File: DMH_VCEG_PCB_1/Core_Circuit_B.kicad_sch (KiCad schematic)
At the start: 104 parts, among them J24 Conn_01x06_PinHeader, J25 Conn_01x10_PinHeader, J26 Conn_01x10_PinHeader, Q17 BC558, Q18 BC558, Q19 BC548, Q20 BC548, Q21 BS170, Q22 BS170, Q23 BC548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

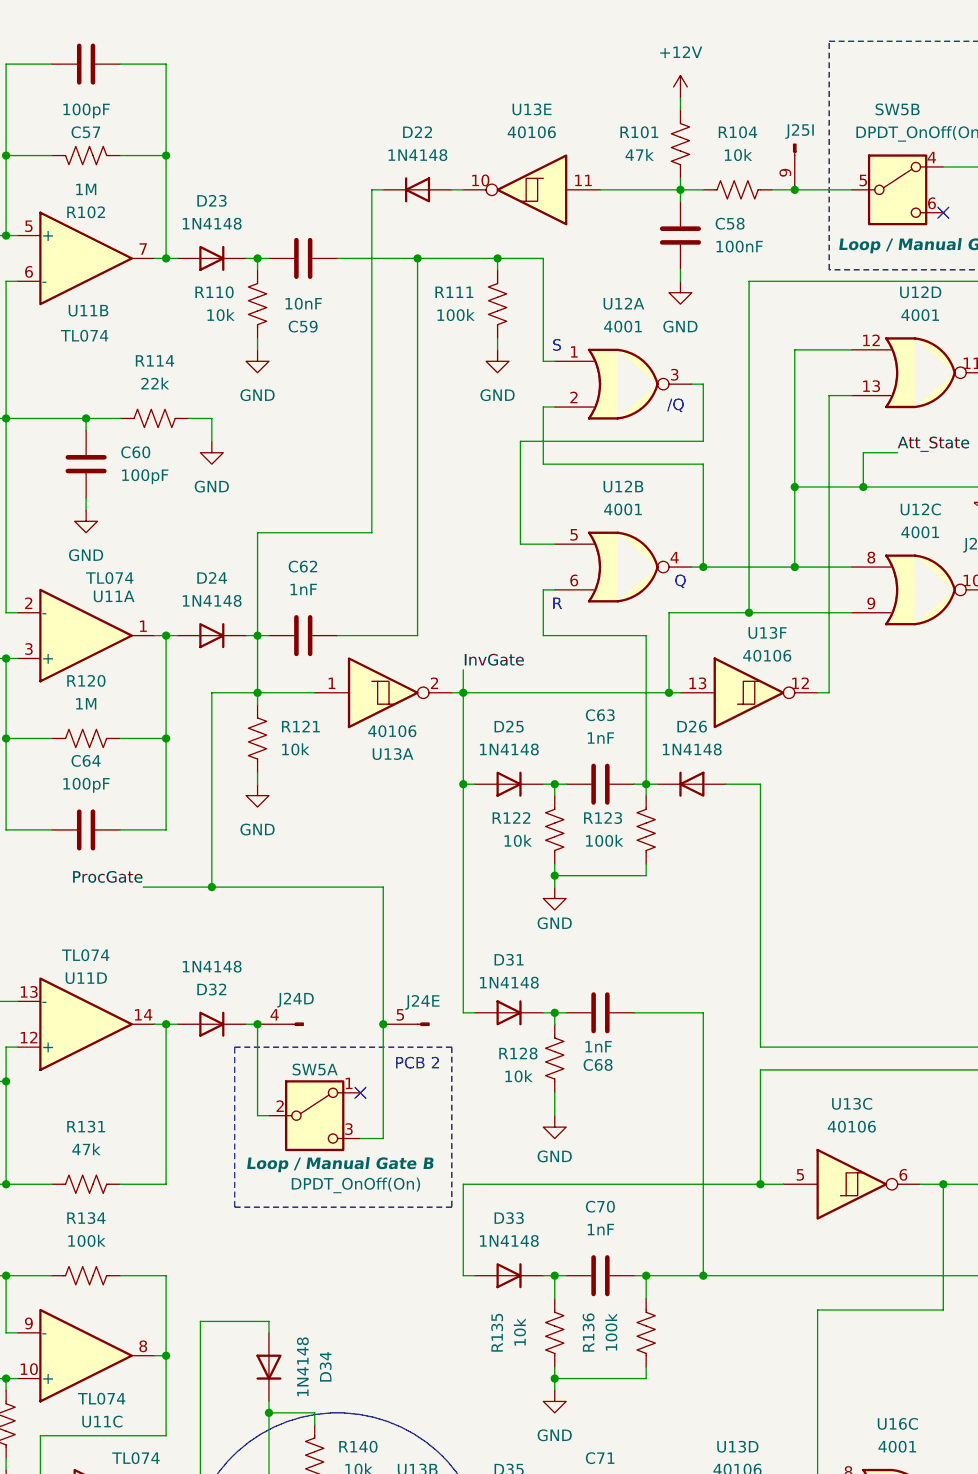
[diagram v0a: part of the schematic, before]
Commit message: Updated PCB 1 with changes from breadboard tests
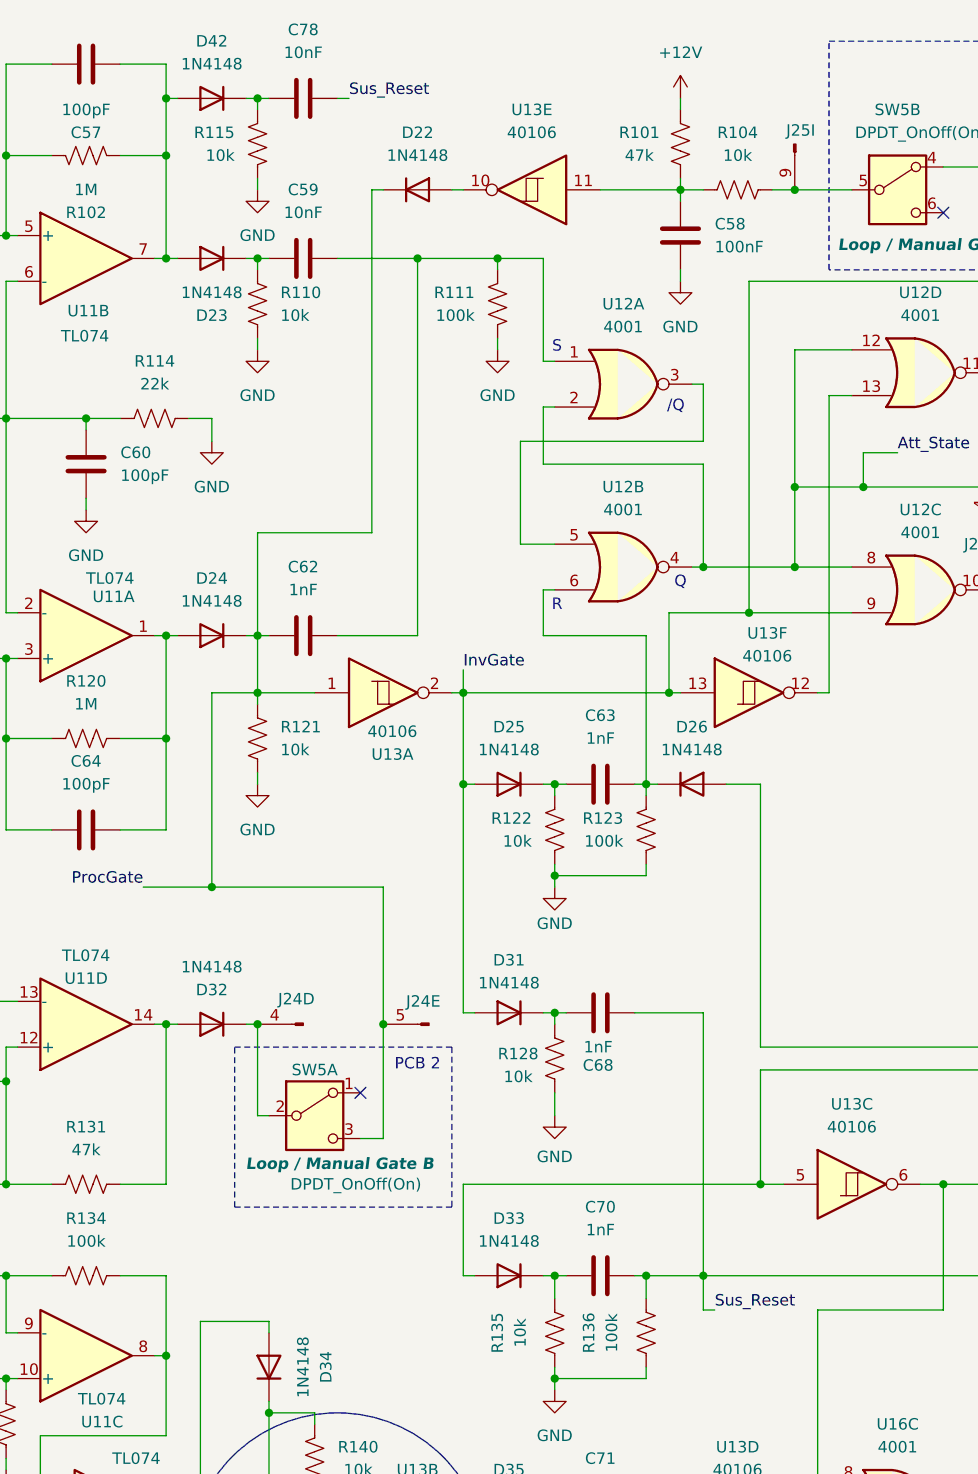
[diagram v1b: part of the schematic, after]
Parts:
- added C78: 10nF, Capacitor_THT:C_Disc_D4.3mm_W1.9mm_P5.00mm, symbol Device:C
- added D42: 1N4148, Diode_THT:D_DO-35_SOD27_P7.62mm_Horizontal, symbol Diode:1N4148
- added R115: 10k, Resistor_THT:R_Axial_DIN0207_L6.3mm_D2.5mm_P7.62mm_Horizontal, symbol Device:R_US
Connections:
- net GND: now also R115.1
- net at C57.2, D23.2 (A), R102.1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: now also D42.2 (A)
- net Sus_Reset: now reaches C68.2, C70.2, R136.1, U16.1
- net Sus_Reset: now also C78.2
- new net: C78.1, D42.1 (K), R115.2
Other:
- moved on the sheet: D23, R110

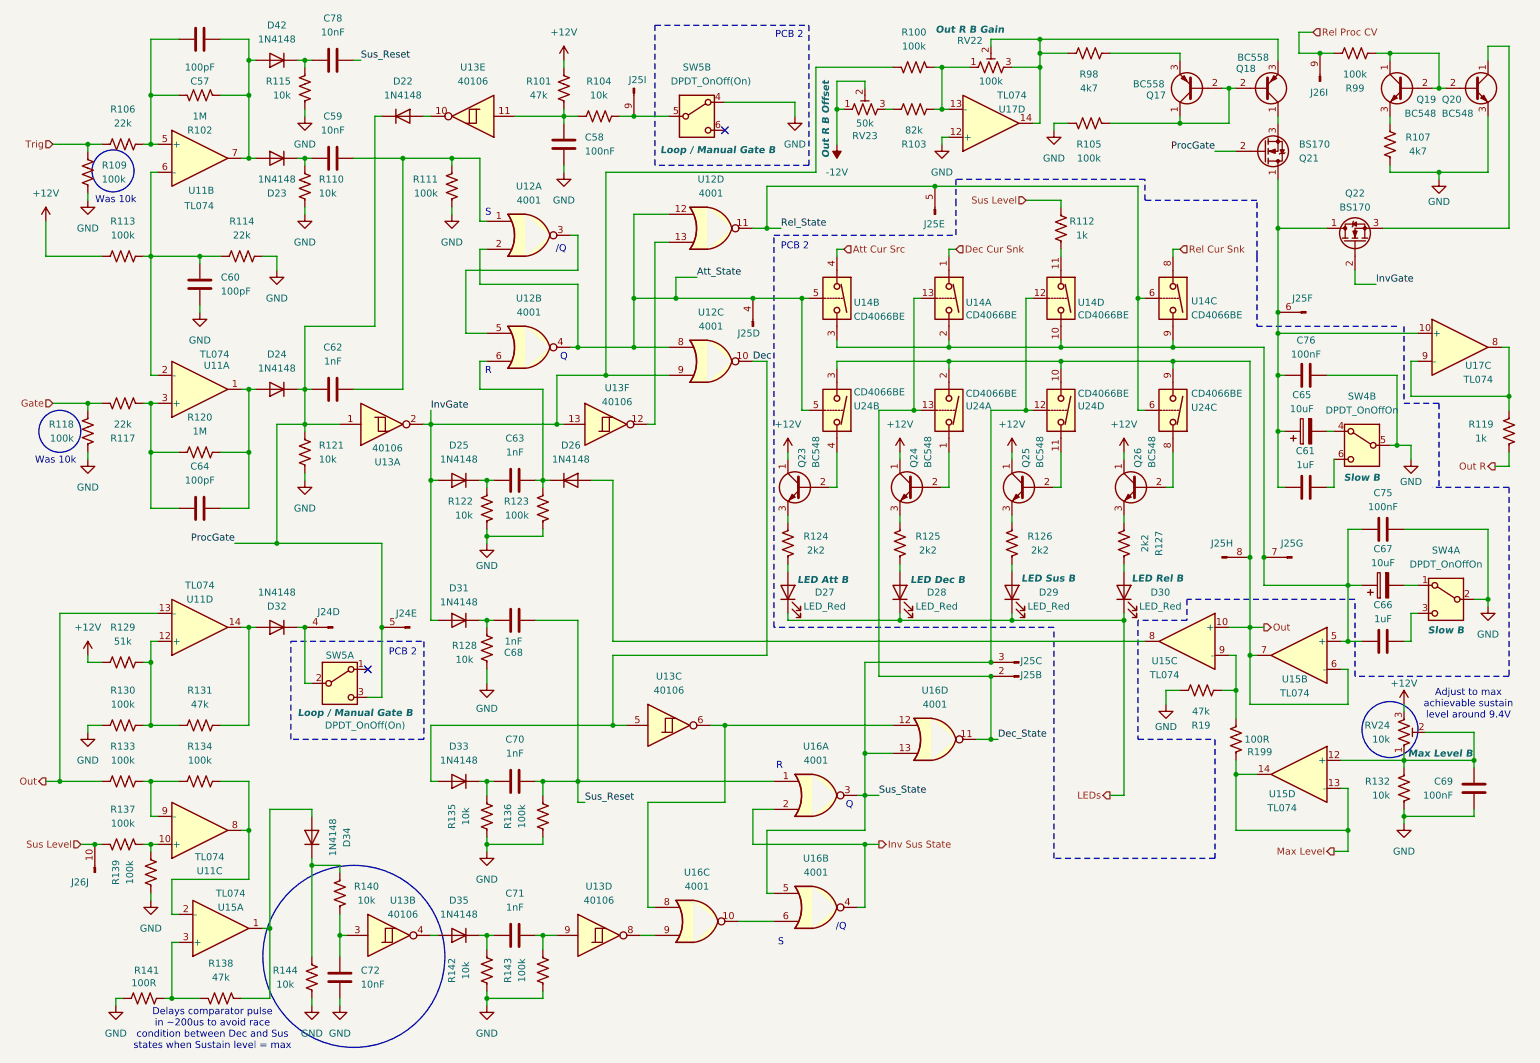
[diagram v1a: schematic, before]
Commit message: Synced A and B changes on PCB 1
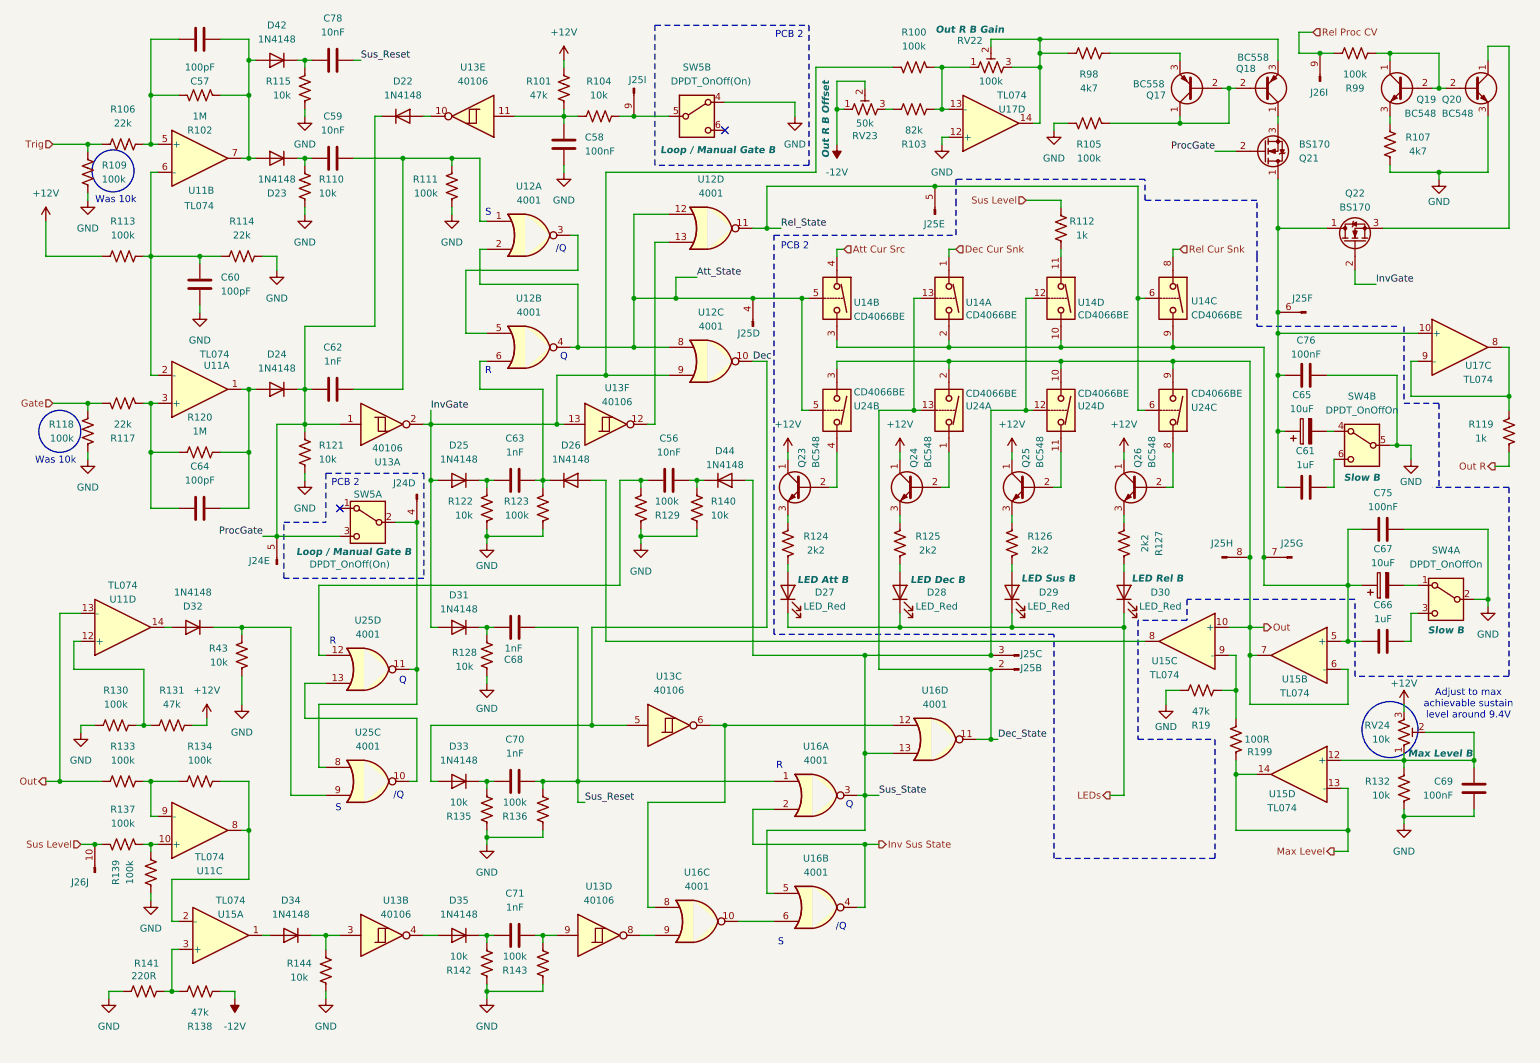
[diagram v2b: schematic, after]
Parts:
- removed C72: 10nF, Capacitor_THT:C_Disc_D4.3mm_W1.9mm_P5.00mm, symbol Device:C
- added C56: 10nF, Capacitor_THT:C_Disc_D4.3mm_W1.9mm_P5.00mm, symbol Device:C
- added D44: 1N4148, Diode_THT:D_DO-35_SOD27_P7.62mm_Horizontal, symbol Diode:1N4148
- added R43: 10k, Resistor_THT:R_Axial_DIN0207_L6.3mm_D2.5mm_P7.62mm_Horizontal, symbol Device:R_US
- added U25: 4001, Package_DIP:DIP-14_W7.62mm_Socket, symbol 4xxx:4001
- R129: value 51k -> 100k
- R141: value 100R -> 220R
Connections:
- net +12V: now also R131.1; no longer R129.2
- net -12V: now also R138.2
- net GND: now also R129.2, R140.1, R43.1
- net Sus_State: now also D44.2 (A)
- net at J24.4 (Pin_4), SW5.2 (B): now also U25.11, U25.8; no longer D32.1 (K)
- net at D32.2 (A), U11.14: no longer R131.1
- net at D34.2 (A), U15.1: no longer R138.2
- net at R130.1, R131.2, U11.12 (+): no longer R129.1
- net at D34.1 (K), R144.1: now also U13.3; no longer R140.1
- net at R140.2: now also C56.2, D44.1 (K); no longer U13.3
- new net: D32.1 (K), R43.2, U25.9
- new net: C56.1, R129.1, U25.12
- new net: U25.10, U25.13
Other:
- note removed: "Delays comparator pulse in ~200us to avoid race condition between Dec and Sus states when Sustain level = max"
- moved on the sheet: C68, D31, D32, D34, J25B, J25C, R128, R130, R131, R135, R136, R138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
